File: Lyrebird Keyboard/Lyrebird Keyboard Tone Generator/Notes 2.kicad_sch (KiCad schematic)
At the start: 80 parts, among them IC15 MC14024BDG, IC16 MC14024BDG, IC17 MC14024BDG, IC18 MC14024BDG, IC19 MC14024BDG, IC20 MC14024BDG

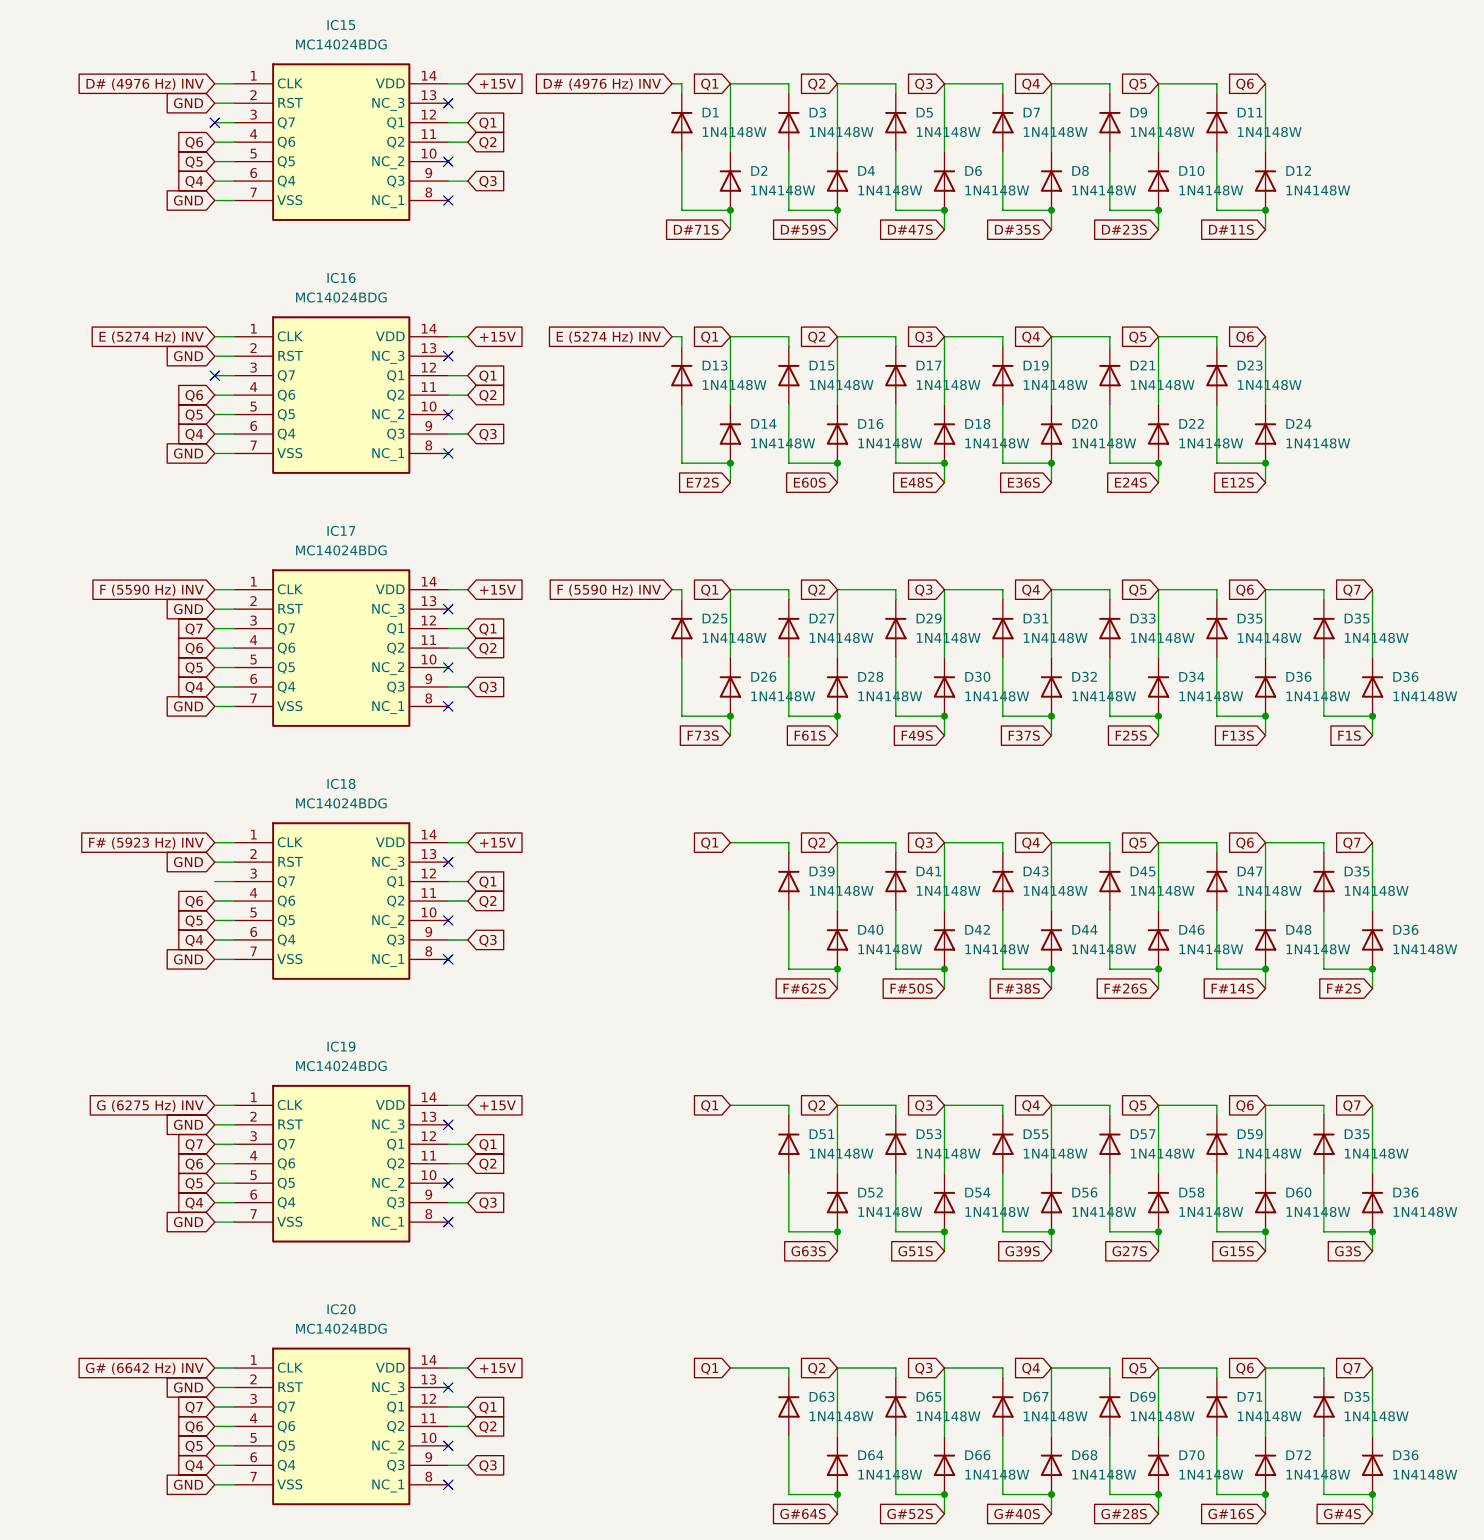
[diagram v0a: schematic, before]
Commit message: Further Tone Generator Work, Diode mixers placed
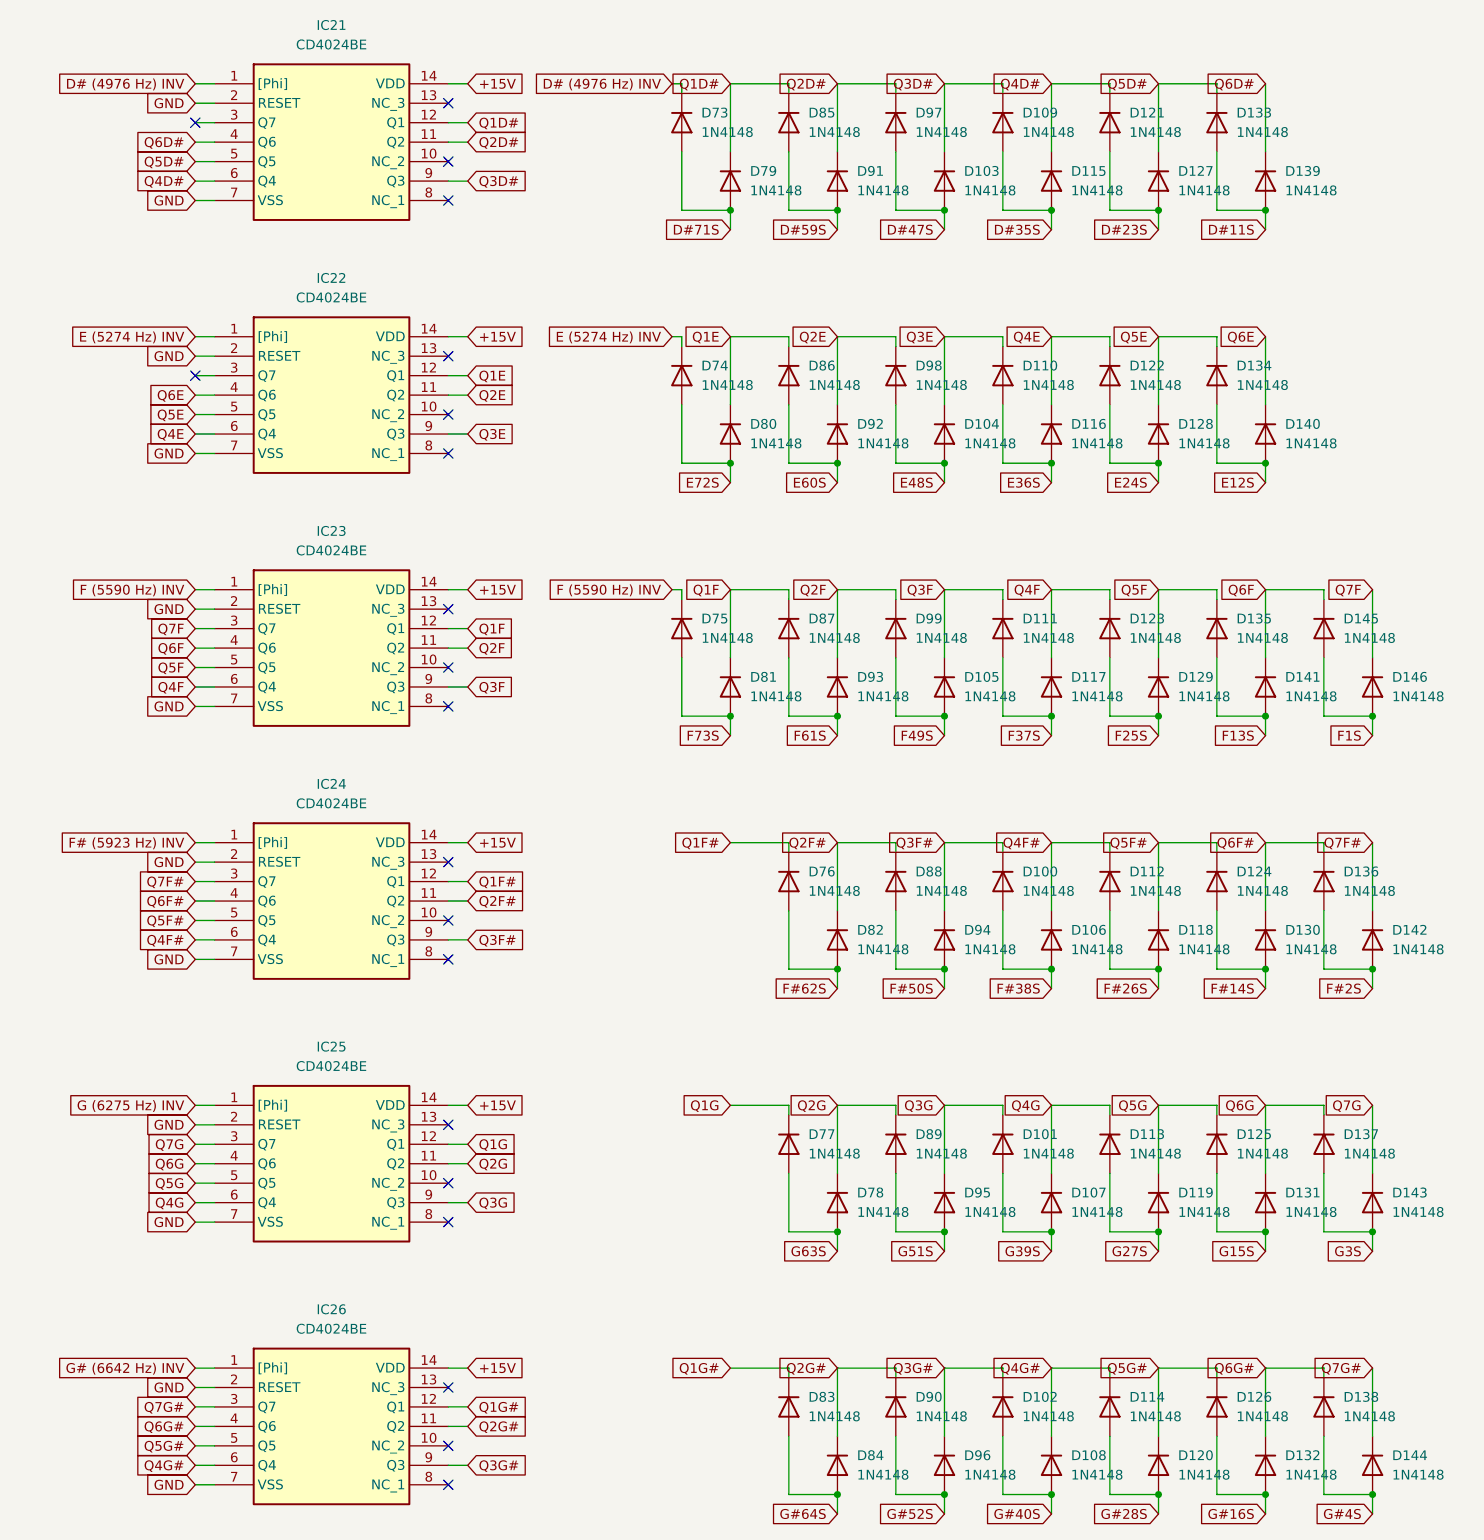
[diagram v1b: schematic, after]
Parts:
- removed D1, D10, D11, D12, D13, D14, D15, D16, D17, D18, D19, D2, D20, D21, D22, D23, D24, D25, D26, D27, D28, D29, D3, D30, D31, D32, D33, D34, D35 (x5), D36 (x5), D39, D4, D40, D41, D42, D43, D44, D45, D46, D47, D48, D5, D51, D52, D53, D54, D55, D56, D57, D58, D59, D6, D60, D63, D64, D65, D66, D67, D68, D69, D7, D70, D71, D72, D8, D9: 1N4148W, Diode_SMD:D_SOD-123, symbol Diode:1N4148W
- removed IC15, IC16, IC17, IC18, IC19, IC20: MC14024BDG, SOIC127P600X175-14N, symbol SamacSys_Parts:MC14024BDG
- added D100, D101, D102, D103, D104, D105, D106, D107, D108, D109, D110, D111, D112, D113, D114, D115, D116, D117, D118, D119, D120, D121, D122, D123, D124, D125, D126, D127, D128, D129, D130, D131, D132, D133, D134, D135, D136, D137, D138, D139, D140, D141, D142, D143, D144, D145, D146, D73, D74, D75, D76, D77, D78, D79, D80, D81, D82, D83, D84, D85, D86, D87, D88, D89, D90, D91, D92, D93, D94, D95, D96, D97, D98, D99: 1N4148, Diode_THT:D_DO-35_SOD27_P7.62mm_Horizontal, symbol Diode:1N4148
- added IC21, IC22, IC23, IC24, IC25, IC26: CD4024BE, DIP794W53P254L1930H508Q14N, symbol SamacSys_Parts:CD4024BE
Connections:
- net +15V: now also IC21.14 (VDD), IC22.14 (VDD), IC23.14 (VDD), IC24.14 (VDD), IC25.14 (VDD), IC26.14 (VDD)
- net D# (4976 Hz) INV: now also D73.1 (K), IC21.1 ([Phi])
- net D#11S: now also D133.2 (A), D139.2 (A)
- net D#23S: now also D121.2 (A), D127.2 (A)
- net D#35S: now also D109.2 (A), D115.2 (A)
- net D#47S: now also D103.2 (A), D97.2 (A)
- net D#59S: now also D85.2 (A), D91.2 (A)
- net D#71S: now also D73.2 (A), D79.2 (A)
- net E (5274 Hz) INV: now also D74.1 (K), IC22.1 ([Phi])
- net E12S: now also D134.2 (A), D140.2 (A)
- net E24S: now also D122.2 (A), D128.2 (A)
- net E36S: now also D110.2 (A), D116.2 (A)
- net E48S: now also D104.2 (A), D98.2 (A)
- net E60S: now also D86.2 (A), D92.2 (A)
- net E72S: now also D74.2 (A), D80.2 (A)
- net F (5590 Hz) INV: now also D75.1 (K), IC23.1 ([Phi])
- net F# (5923 Hz) INV: now also IC24.1 ([Phi])
- net F#14S: now also D124.2 (A), D130.2 (A)
- net F#26S: now also D112.2 (A), D118.2 (A)
- net F#2S: now also D136.2 (A), D142.2 (A)
- net F#38S: now also D100.2 (A), D106.2 (A)
- net F#50S: now also D88.2 (A), D94.2 (A)
- net F#62S: now also D76.2 (A), D82.2 (A)
- net F13S: now also D135.2 (A), D141.2 (A)
- net F1S: now also D145.2 (A), D146.2 (A)
- net F25S: now also D123.2 (A), D129.2 (A)
- net F37S: now also D111.2 (A), D117.2 (A)
- net F49S: now also D105.2 (A), D99.2 (A)
- net F61S: now also D87.2 (A), D93.2 (A)
- net F73S: now also D75.2 (A), D81.2 (A)
- net G (6275 Hz) INV: now also IC25.1 ([Phi])
- net G# (6642 Hz) INV: now also IC26.1 ([Phi])
- net G#16S: now also D126.2 (A), D132.2 (A)
- net G#28S: now also D114.2 (A), D120.2 (A)
- net G#40S: now also D102.2 (A), D108.2 (A)
- net G#4S: now also D138.2 (A), D144.2 (A)
- net G#52S: now also D90.2 (A), D96.2 (A)
- net G#64S: now also D83.2 (A), D84.2 (A)
- net G15S: now also D125.2 (A), D131.2 (A)
- net G27S: now also D113.2 (A), D119.2 (A)
- net G39S: now also D101.2 (A), D107.2 (A)
- net G3S: now also D137.2 (A), D143.2 (A)
- net G51S: now also D89.2 (A), D95.2 (A)
- net G63S: now also D77.2 (A), D78.2 (A)
- net GND: now also IC21.2 (RESET), IC21.7 (VSS), IC22.2 (RESET), IC22.7 (VSS), IC23.2 (RESET), IC23.7 (VSS), IC24.2 (RESET), IC24.7 (VSS), IC25.2 (RESET), IC25.7 (VSS), IC26.2 (RESET), IC26.7 (VSS)
- new net Q1D#: D79.1 (K), D85.1 (K), IC21.12 (Q1)
- new net Q1E: D80.1 (K), D86.1 (K), IC22.12 (Q1)
- new net Q1F: D81.1 (K), D87.1 (K), IC23.12 (Q1)
- new net Q1F#: D76.1 (K), IC24.12 (Q1)
- new net Q1G: D77.1 (K), IC25.12 (Q1)
- new net Q1G#: D83.1 (K), IC26.12 (Q1)
- new net Q2D#: D91.1 (K), D97.1 (K), IC21.11 (Q2)
- new net Q2E: D92.1 (K), D98.1 (K), IC22.11 (Q2)
- new net Q2F: D93.1 (K), D99.1 (K), IC23.11 (Q2)
- new net Q2F#: D82.1 (K), D88.1 (K), IC24.11 (Q2)
- new net Q2G: D78.1 (K), D89.1 (K), IC25.11 (Q2)
- new net Q2G#: D84.1 (K), D90.1 (K), IC26.11 (Q2)
- new net Q3D#: D103.1 (K), D109.1 (K), IC21.9 (Q3)
- new net Q3E: D104.1 (K), D110.1 (K), IC22.9 (Q3)
- new net Q3F: D105.1 (K), D111.1 (K), IC23.9 (Q3)
- new net Q3F#: D100.1 (K), D94.1 (K), IC24.9 (Q3)
- new net Q3G: D101.1 (K), D95.1 (K), IC25.9 (Q3)
- new net Q3G#: D102.1 (K), D96.1 (K), IC26.9 (Q3)
- new net Q4D#: D115.1 (K), D121.1 (K), IC21.6 (Q4)
- new net Q4E: D116.1 (K), D122.1 (K), IC22.6 (Q4)
- new net Q4F: D117.1 (K), D123.1 (K), IC23.6 (Q4)
- new net Q4F#: D106.1 (K), D112.1 (K), IC24.6 (Q4)
- new net Q4G: D107.1 (K), D113.1 (K), IC25.6 (Q4)
- new net Q4G#: D108.1 (K), D114.1 (K), IC26.6 (Q4)
- new net Q5D#: D127.1 (K), D133.1 (K), IC21.5 (Q5)
- new net Q5E: D128.1 (K), D134.1 (K), IC22.5 (Q5)
- new net Q5F: D129.1 (K), D135.1 (K), IC23.5 (Q5)
- new net Q5F#: D118.1 (K), D124.1 (K), IC24.5 (Q5)
- new net Q5G: D119.1 (K), D125.1 (K), IC25.5 (Q5)
- new net Q5G#: D120.1 (K), D126.1 (K), IC26.5 (Q5)
- new net Q6D#: D139.1 (K), IC21.4 (Q6)
- new net Q6E: D140.1 (K), IC22.4 (Q6)
- new net Q6F: D141.1 (K), D145.1 (K), IC23.4 (Q6)
- new net Q6F#: D130.1 (K), D136.1 (K), IC24.4 (Q6)
- new net Q6G: D131.1 (K), D137.1 (K), IC25.4 (Q6)
- new net Q6G#: D132.1 (K), D138.1 (K), IC26.4 (Q6)
- new net Q7F: D146.1 (K), IC23.3 (Q7)
- new net Q7F#: D142.1 (K), IC24.3 (Q7)
- new net Q7G: D143.1 (K), IC25.3 (Q7)
- new net Q7G#: D144.1 (K), IC26.3 (Q7)
